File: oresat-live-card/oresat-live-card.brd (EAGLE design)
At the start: 99.8 x 94.6 mm, 322 parts, among them J1 ORESAT-DEBUG-CONNECTOR-CARD, J100 DM3BT-DSF-PEJS, J102 FTSH-105-XX-X-DV-K, J2 SM06B-SRSS-TB(LF)(SN), J4 TFM-120-01-L-D-RA, Q1 MMBT2907, Q2 PMV45EN, Q3 DMP2240UDM, Q4 PMV45EN, Q5 MOSFET-PCH-SOT23-6, Q6 MOSFET-PCH-SOT23-6, U1 RCLAMP0504FB, U10 TLVH431, U11 TCAN330, U12 MIC842LYC5, U13 MIC842LYC5, U14 MAX4211FETE, U15 TPS62112, U16 MAX7310ATE, U17 25AAXX, U18 RCLAMP0504FB, U19 TQP9111, U2 TPS2051CDBVR, U3 THGBMJG7C2LBAU8, U4 SN74LVC1G07DCK, U5 TPS62112, U6 SN74LVC1G32QDBVRQ1, U7 OSD3358-512M-BSM, U8 MIC94090YC6-TR, Y1 24MHz, Y2 ABS07-32.768KHZ-T

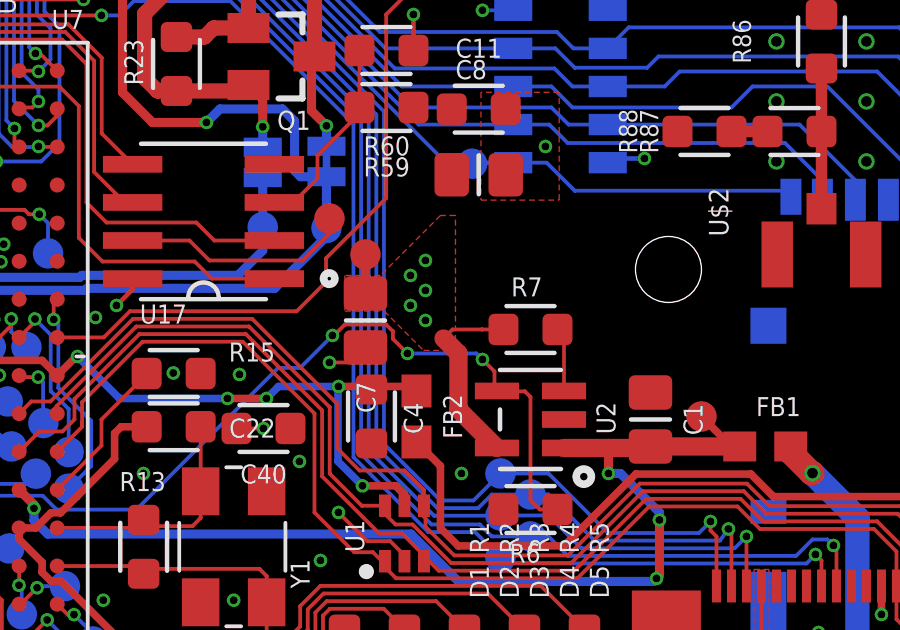
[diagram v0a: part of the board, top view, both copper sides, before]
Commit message: tracked down and routed a VDD airwire
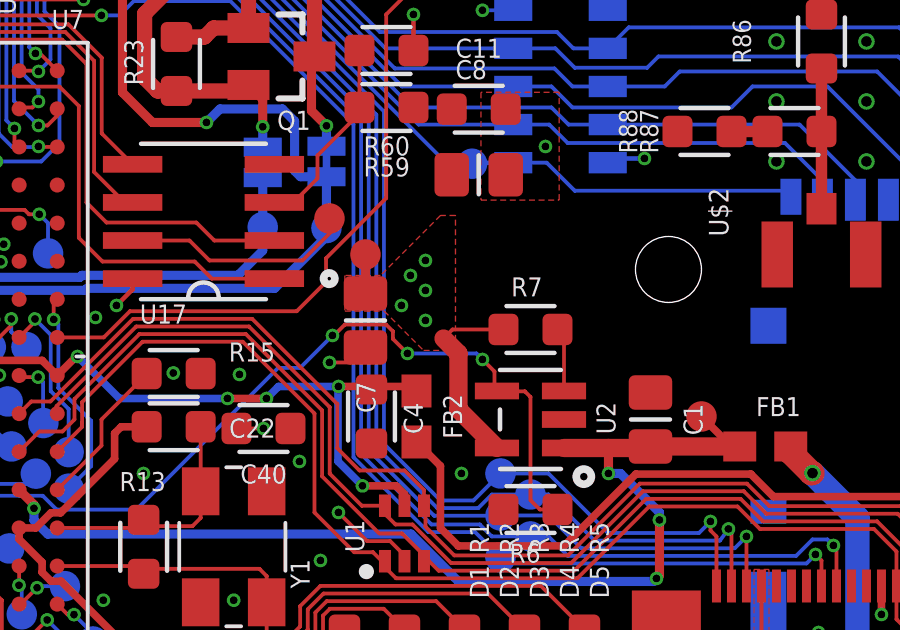
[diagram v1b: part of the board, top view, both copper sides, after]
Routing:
- net VDD: track 7.88 -> 32.6 mm

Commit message: Added 5V_PA polygon, did some OCD cleanup on RF sheet, yelled at Nick a lot.
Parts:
- removed RT1: NTCTHERMISTER, R-Generic-Thermister0402:R0402
- added RT2: TDK NTCG163JX103DT1S, apdm:0603-THERMISTOR-B
- LED2: device SamacSys_Parts:LEDC1607X80N -> oresat-samacsys_Parts:LEDC1607X80N
- moved C47 1.77 mm to (81.2, 40.4), turned to 0 degrees
- moved C23 1.12 mm to (80.4, 45.7)
- moved R18 1.12 mm to (82.2, 45.7)
- moved TP179 1.12 mm to (82.2, 43.5)
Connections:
- net GND: now also RT2.2; no longer RT1.1
- net PA_THERMISTOR: now also RT2.1; no longer RT1.2
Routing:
- net 5V_PA: track 71.9 -> 11.0 mm
- net PA_THERMISTOR: track 58.6 -> 55.8 mm
- net 1.8V-L: track 90.2 -> 88.1 mm
- added copper zone on layer 15, net 5V_PA

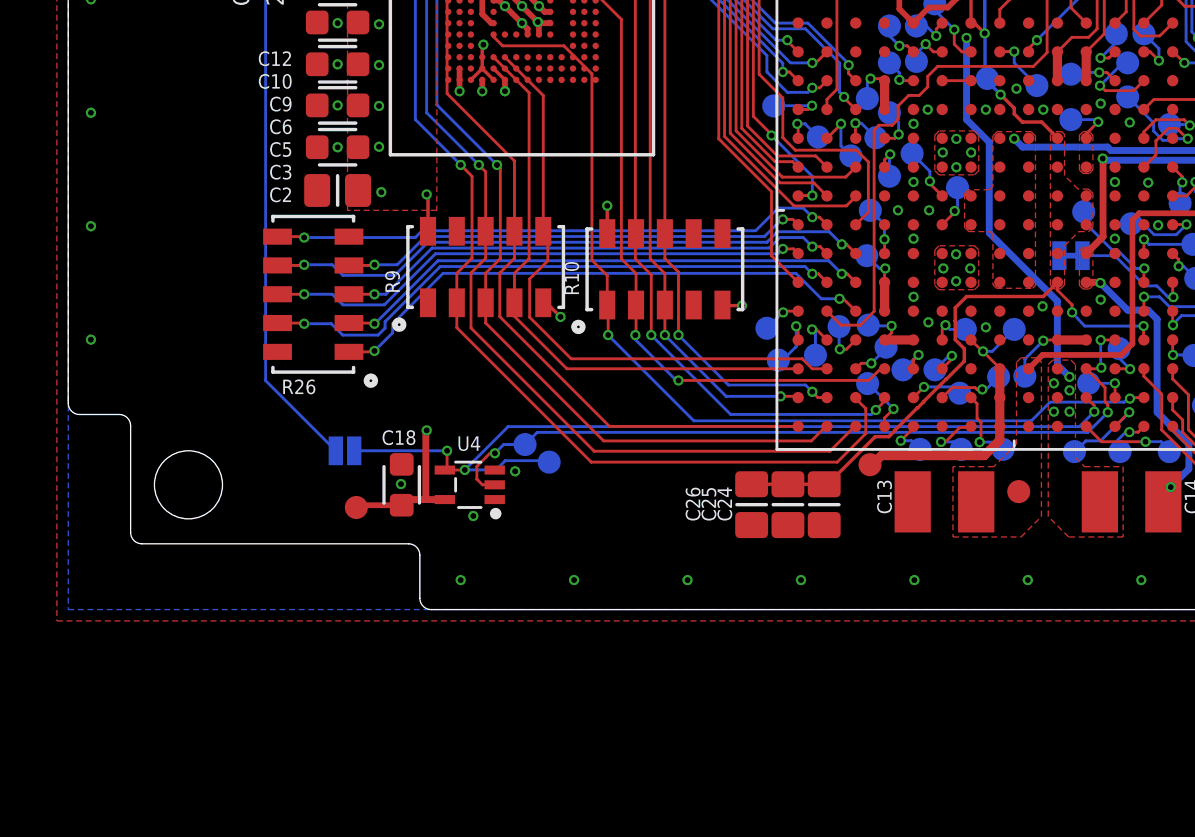
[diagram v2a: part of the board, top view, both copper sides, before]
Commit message: Seperated the digital and analog 1.8V rails
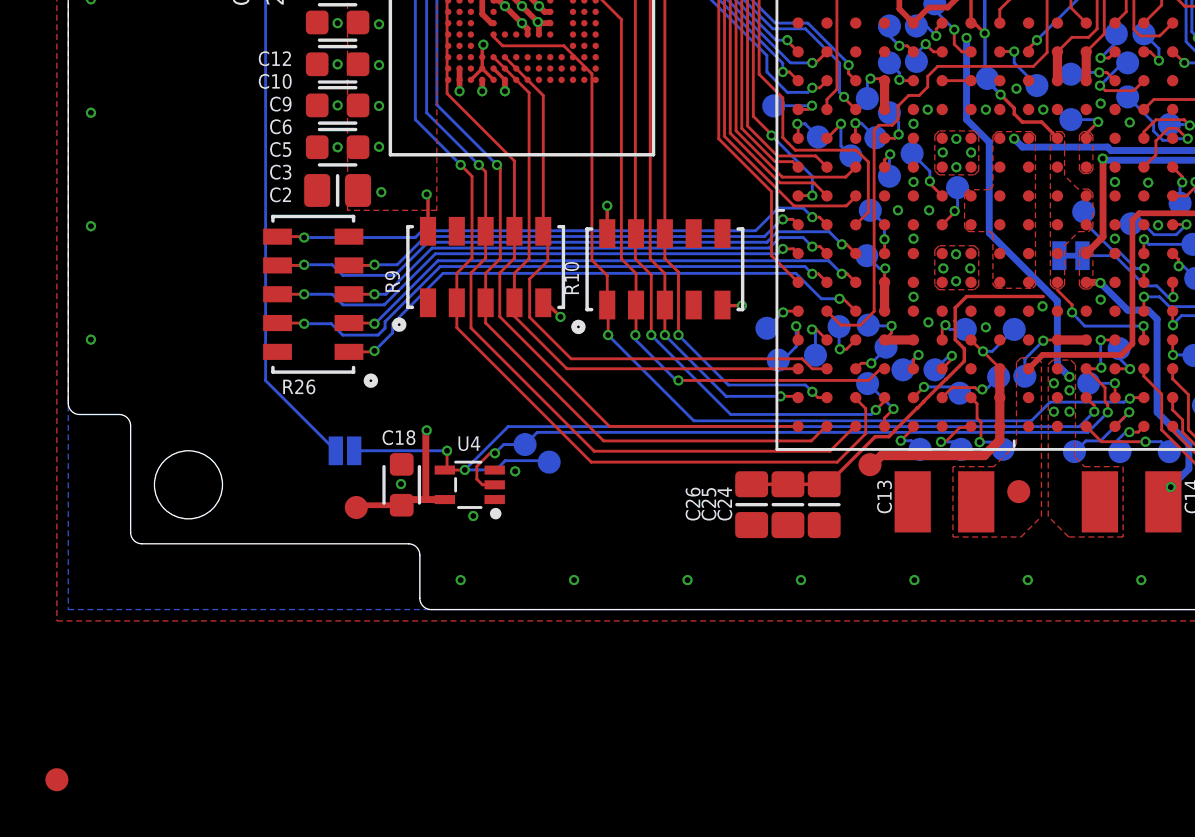
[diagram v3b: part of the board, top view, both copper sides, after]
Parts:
- added TP8: TEST-POINT3X4, SparkFun-Connectors:PAD.03X.04
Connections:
- removed net 1.8V-L: C24.1, C25.1, C26.1, R18.1, TP171.P$1, U7.A7, U7.B7, U7.F10, U7.G10, U7.H10, U7.H11, U7.J10, U7.J11, U7.K10, U7.L10, U7.N13
- new net 1.8V: C24.1, C25.1, C26.1, R18.1, TP171.P$1, TP8.P$1, U7.A7, U7.B7, U7.N13
- new net N$3: U7.F10, U7.G10, U7.H10, U7.H11, U7.J10, U7.J11, U7.K10, U7.L10
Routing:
- net 1.8V-L: track 88.1 -> 0.00 mm, vias 5 -> 0
- net 1.8V: track 0.00 -> 86.8 mm, vias 0 -> 5
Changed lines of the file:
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@@
 <?xml version="1.0" encoding="utf-8"?>
 <!DOCTYPE eagle SYSTEM "eagle.dtd">
-<eagle version="9.6.1">
+<eagle version="9.6.2">
 <drawing>
 <settings>
@@
 <attribute name="DPN" value="THGBMJG7C2LBAU8-ND" x="20" y="26.6" size="1.778" layer="27" display="off"/>
 <attribute name="MPN" value="THGBMJG7C2LBAU8" x="20" y="26.6" size="1.778" layer="27" display="off"/>
-<attribute name="NAME" x="13.025" y="32.2125" size="0.635" layer="25" font="vector" ratio="20"/>
 <attribute name="NAME" x="20" y="26.6" size="1.5" layer="33" ratio="15" align="center"/>
+<attribute name="NAME" x="13.025" y="32.2125" size="0.635" layer="25" font="vector" ratio="20"/>
 <attribute name="VALUE" x="14.4" y="19" size="0.8" layer="27" font="vector" ratio="15"/>
 </element>
@@
 <attribute name="MFR" value="Coilcraft" x="77.15" y="33.3" size="1.778" layer="27" rot="R180" display="off"/>
 <attribute name="MPN" value="0402DC-1N7XJRU" x="77.15" y="33.3" size="1.778" layer="27" rot="R180" display="off"/>
-<attribute name="NAME" x="79.65" y="33.5" size="0.635" layer="25" font="vector" ratio="20" rot="R180"/>
 <attribute name="NAME" x="77.15" y="33.3" size="0.2" layer="33" ratio="15" rot="R180" align="center"/>
+<attribute name="NAME" x="79.65" y="33.5" size="0.635" layer="25" font="vector" ratio="20" rot="R180"/>
 <attribute name="VALUE" x="77.85" y="34.7" size="0.8" layer="27" font="vector" ratio="15" rot="R180"/>
 </element>
@@
 <attribute name="MFR" value="Coilcraft" x="72.8" y="36.9" size="1.778" layer="27" rot="R270" display="off"/>
 <attribute name="MPN" value="0805CS-060XJLC" x="72.8" y="36.9" size="1.778" layer="27" rot="R270" display="off"/>
-<attribute name="NAME" x="71.95" y="35.75" size="0.635" layer="25" font="vector" ratio="20" rot="R90"/>
 <attribute name="NAME" x="72.8" y="36.9" size="0.4" layer="33" ratio="15" rot="R270" align="center"/>
+<attribute name="NAME" x="71.95" y="35.75" size="0.635" layer="25" font="vector" ratio="20" rot="R90"/>
 <attribute name="VALUE" x="71.15" y="38.15" size="0.8" layer="27" font="vector" ratio="15" rot="R270"/>
 </element>
@@
 <attribute name="MFR" value="TDK Corporation" x="76.7" y="45.5" size="1.778" layer="27" rot="R90" display="off"/>
 <attribute name="MPN" value="MLK1005S1N0ST000" x="76.7" y="45.5" size="1.778" layer="27" rot="R90" display="off"/>
-<attribute name="NAME" x="76.7" y="45.5" size="0.2" layer="33" ratio="15" rot="R90" align="center"/>
 <attribute name="NAME" x="79.45" y="45.2" size="0.635" layer="25" font="vector" ratio="20" rot="R90"/>
+<attribute name="NAME" x="76.7" y="45.5" size="0.2" layer="33" ratio="15" rot="R90" align="center"/>
 <attribute name="VALUE" x="77.95" y="44.8" size="0.8" layer="27" font="vector" ratio="15" rot="R90"/>
 </element>
@@
 <attribute name="MFR" value="Vishay / Dale" x="76.7" y="36.5" size="1.778" layer="27" rot="R90" display="off"/>
 <attribute name="MPN" value="CRCW04023R30FKED" x="76.7" y="36.5" size="1.778" layer="27" rot="R90" display="off"/>
-<attribute name="NAME" x="79.45" y="36.2" size="0.635" layer="25" font="vector" ratio="20" rot="R90"/>
 <attribute name="NAME" x="76.7" y="36.5" size="0.2" layer="33" ratio="15" rot="R90" align="center"/>
+<attribute name="NAME" x="79.45" y="36.2" size="0.635" layer="25" font="vector" ratio="20" rot="R90"/>
 <attribute name="VALUE" x="77.95" y="35.8" size="0.8" layer="27" font="vector" ratio="15" rot="R90"/>
 </element>
@@
 <attribute name="VALUE" x="81.2" y="43.5" size="0.8" layer="27" font="vector" ratio="15" rot="R180" align="top-left"/>
 </element>
+<element name="TP8" library="SparkFun-Connectors" package="PAD.03X.04" value="TEST-POINT3X4" x="-0.5" y="-7.5" smashed="yes"/>
 </elements>
 <signals>
@@
 </signal>
 <signal name="1.8V-L">
+<polygon width="0.127" layer="1">
+<vertex x="43.79375" y="21.06875"/>
+<vertex x="43.45" y="21.06875"/>
+<vertex x="43.29375" y="20.9125"/>
+<vertex x="43.29375" y="14.31875"/>
+<vertex x="43.48125" y="14.13125"/>
+<vertex x="43.73125" y="14.13125"/>
+<vertex x="43.91875" y="14.31875"/>
+<vertex x="43.91875" y="16.0375"/>
+<vertex x="44.54375" y="16.6625"/>
+<vertex x="44.98125" y="16.6625"/>
+<vertex x="45.16875" y="16.85"/>
+<vertex x="45.16875" y="18.35"/>
+<vertex x="44.98125" y="18.5375"/>
+<vertex x="44.5125" y="18.5375"/>
+<vertex x="43.91875" y="19.13125"/>
+<vertex x="43.91875" y="20.94375"/>
+</polygon>
+</signal>
+<signal name="N$1">
+<contactref element="U7" pad="D7"/>
+<contactref element="U7" pad="D6"/>
+<wire x1="38.525" y1="23.315" x2="39.795" y2="23.315" width="0.127" layer="1"/>
+</signal>
+<signal name="N$3">
 <contactref element="U7" pad="F10"/>
 <contactref element="U7" pad="G10"/>
@@
 <contactref element="U7" pad="K10"/>
 <contactref element="U7" pad="L10"/>
+<wire x1="43.605" y1="19.505" x2="43.605" y2="20.775" width="0" layer="19" extent="1-1"/>
+<wire x1="43.605" y1="18.235" x2="43.605" y2="19.505" width="0" layer="19" extent="1-1"/>
+<wire x1="44.875" y1="18.235" x2="43.605" y2="18.235" width="0" layer="19" extent="1-1"/>
+<wire x1="43.605" y1="16.965" x2="43.605" y2="18.235" width="0" layer="19" extent="1-1"/>
+<wire x1="44.875" y1="16.965" x2="44.875" y2="18.235" width="0" layer="19" extent="1-1"/>
+<wire x1="43.605" y1="15.695" x2="43.605" y2="16.965" width="0" layer="19" extent="1-1"/>
+<wire x1="43.605" y1="14.425" x2="43.605" y2="15.695" width="0" layer="19" extent="1-1"/>
+</signal>
+<signal name="1.8V">
 <contactref element="U7" pad="A7"/>
 <contactref element="C26" pad="1"/>
@@
 <wire x1="30.125" y1="5.525" x2="31.725" y2="5.525" width="0.1524" layer="1"/>
 <wire x1="31.725" y1="5.525" x2="33.325" y2="5.525" width="0.1524" layer="1"/>
-<wire x1="43.605" y1="20.775" x2="43.605" y2="20.795" width="0.1524" layer="1"/>
 <wire x1="43.605" y1="20.795" x2="42.9082" y2="21.4918" width="0.1524" layer="1"/>
 <wire x1="42.9082" y1="21.4918" x2="42.05911875" y2="21.4918" width="0.1524" layer="1"/>
@@
 <wire x1="41.7" y1="22.1" x2="41.7" y2="21.85091875" width="0.1524" layer="1"/>
 <wire x1="42.05911875" y1="21.4918" x2="41.7" y2="21.85091875" width="0.1524" layer="1"/>
-<wire x1="43.605" y1="14.425" x2="42.98" y2="13.8" width="0.1524" layer="1"/>
 <wire x1="42.98" y1="13.8" x2="39.6" y2="13.8" width="0.1524" layer="1"/>
 <wire x1="39.6" y1="13.8" x2="39.1" y2="13.3" width="0.1524" layer="1"/>
@@
 <wire x1="81.8" y1="45.3" x2="82.2" y2="45.7" width="0.1524" layer="16"/>
 <via x="82.2" y="45.7" extent="1-16" drill="0.254"/>
+<contactref element="R18" pad="1"/>
 <contactref element="U7" pad="N13"/>
+<contactref element="TP8" pad="P$1"/>
 <wire x1="47.415" y1="11.885" x2="47.4" y2="11.9" width="0.127" layer="1"/>
 <wire x1="47.4" y1="11.9" x2="47.4" y2="12.5" width="0.127" layer="1"/>
@@
 <wire x1="44.25" y1="13.4329625" x2="43.605" y2="14.0779625" width="0.127" layer="1"/>
 <wire x1="44.25" y1="13.4329625" x2="44.25" y2="13.1" width="0.127" layer="1"/>
-<wire x1="43.605" y1="14.425" x2="43.605" y2="14.0779625" width="0.127" layer="1"/>
-<polygon width="0.127" layer="1">
-<vertex x="43.79375" y="21.06875"/>
-<vertex x="43.45" y="21.06875"/>
-<vertex x="43.29375" y="20.9125"/>
-<vertex x="43.29375" y="14.31875"/>
-<vertex x="43.48125" y="14.13125"/>
-<vertex x="43.73125" y="14.13125"/>
-<vertex x="43.91875" y="14.31875"/>
-<vertex x="43.91875" y="16.0375"/>
-<vertex x="44.54375" y="16.6625"/>
-<vertex x="44.98125" y="16.6625"/>
-<vertex x="45.16875" y="16.85"/>
-<vertex x="45.16875" y="18.35"/>
-<vertex x="44.98125" y="18.5375"/>
-<vertex x="44.5125" y="18.5375"/>
-<vertex x="43.91875" y="19.13125"/>
-<vertex x="43.91875" y="20.94375"/>
-</polygon>
-<contactref element="R18" pad="1"/>
 <wire x1="82.2" y1="45.7" x2="82.2" y2="46.6" width="0" layer="19" extent="1-1"/>
-</signal>
-<signal name="N$1">
-<contactref element="U7" pad="D7"/>
-<contactref element="U7" pad="D6"/>
-<wire x1="38.525" y1="23.315" x2="39.795" y2="23.315" width="0.127" layer="1"/>
+<wire x1="43.605" y1="14.0779625" x2="43.605" y2="20.795" width="0" layer="19" extent="1-1"/>
+<wire x1="42.98" y1="13.8" x2="43.605" y2="14.0779625" width="0" layer="19" extent="1-1"/>
+<wire x1="-0.5" y1="-7.5" x2="30.125" y2="5.525" width="0" layer="19" extent="1-1"/>
 </signal>
 </signals>
